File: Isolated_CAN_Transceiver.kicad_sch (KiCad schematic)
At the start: 6 parts, among them SW1 SW_DIP_x01, U4 ISO1050DUB

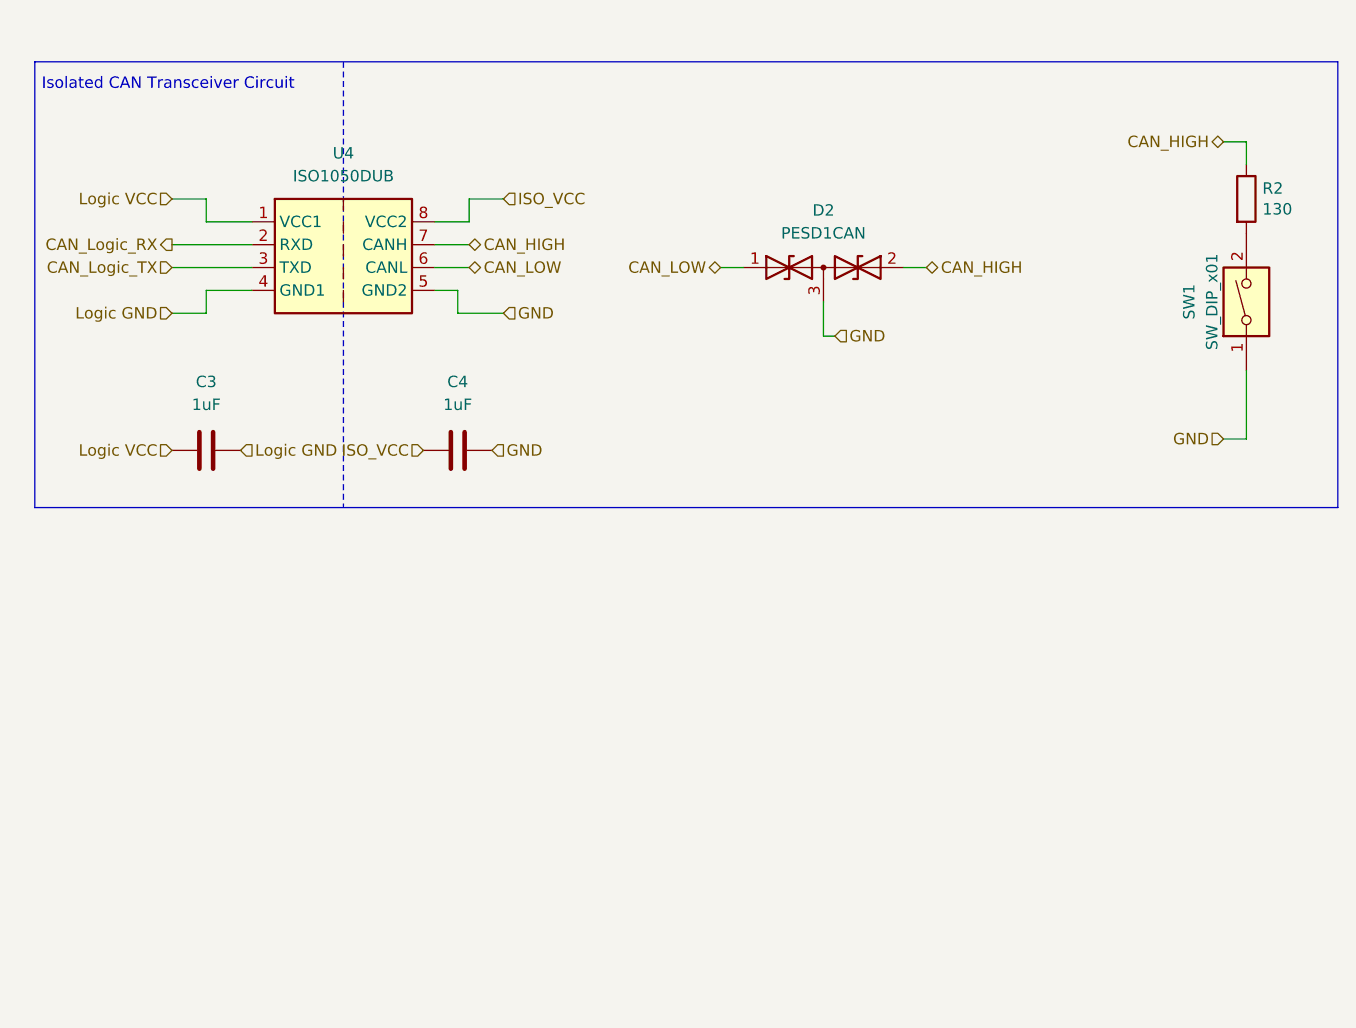
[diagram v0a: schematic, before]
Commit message: Updated Isolated CANTX
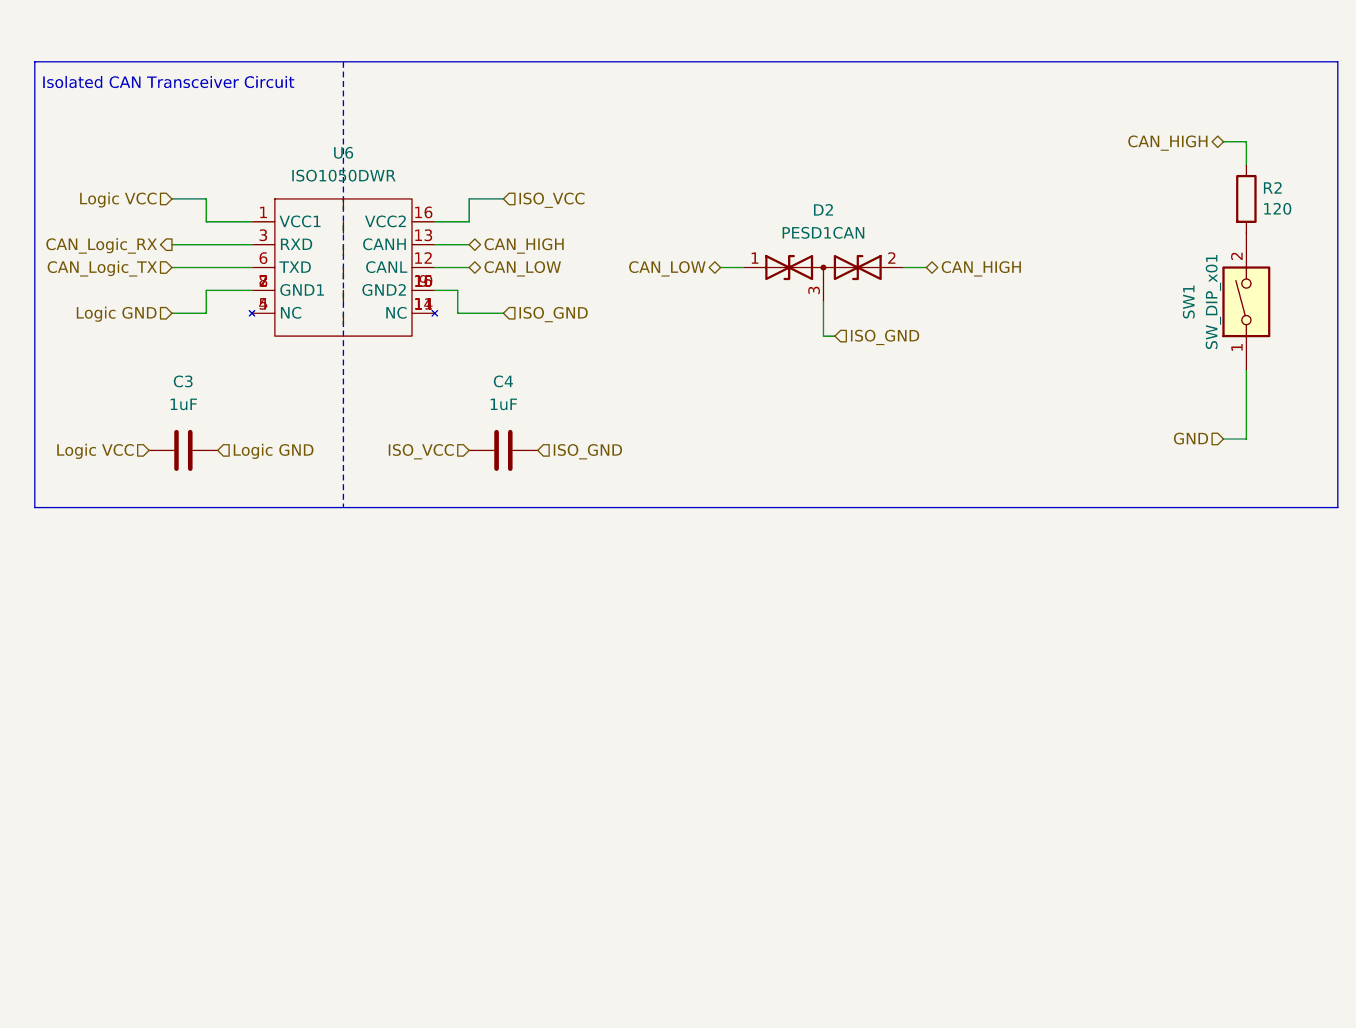
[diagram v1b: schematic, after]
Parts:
- removed U4: ISO1050DUB, Package_SO:SOP-8_6.62x9.15mm_P2.54mm, symbol Interface_CAN_LIN:ISO1050DUB
- added U6: ISO1050DWR, Package_SO:SOP-16_4.55x10.3mm_P1.27mm, symbol user:ISO1050DWR
- R2: value 130 -> 120
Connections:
- net CAN_HIGH: now also U6.13 (CANH)
- net CAN_LOW: now also U6.12 (CANL)
- net CAN_Logic_RX: now also U6.3 (RXD)
- net CAN_Logic_TX: now also U6.6 (TXD)
- net GND: no longer C4.1, D2.3 (common)
- net ISO_VCC: now also U6.16 (VCC2)
- net Logic GND: now also U6.2 (GND1), U6.7 (GND1), U6.8 (GND1)
- net Logic VCC: now also U6.1 (VCC1)
- new net: U6.11 (NC), U6.14 (NC)
- new net: U6.4 (NC), U6.5 (NC)
- new net ISO_GND: C4.1, D2.3 (common), U6.10 (GND2), U6.15 (GND2), U6.9 (GND2)
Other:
- moved on the sheet: C3, C4
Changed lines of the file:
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@@
 	(hierarchical_label "Logic VCC"
 		(shape input)
-		(at 85.09 97.79 180)
+		(at 82.55 97.79 180)
 		(effects
 			(font
@@
 		)
 	)
-	(hierarchical_label "GND"
+	(hierarchical_label "ISO_GND"
 		(shape input)
 		(at 158.75 85.09 0)
@@
 		)
 	)
-	(hierarchical_label "GND"
+	(hierarchical_label "ISO_GND"
 		(shape input)
 		(at 121.92 82.55 0)
@@
 	(hierarchical_label "ISO_VCC"
 		(shape input)
-		(at 113.03 97.79 180)
-		(effects
-			(font
-				(size 1.27 1.27)
-			)
-			(justify right)
-		)
-	)
-	(hierarchical_label "GND"
-		(shape input)
-		(at 120.65 97.79 0)
+		(at 118.11 97.79 180)
+		(effects
+			(font
+				(size 1.27 1.27)
+			)
+			(justify right)
+		)
+	)
+	(hierarchical_label "ISO_GND"
+		(shape input)
+		(at 125.73 97.79 0)
 		(effects
 			(font
@@
 	(hierarchical_label "Logic GND"
 		(shape input)
-		(at 92.71 97.79 0)
+		(at 90.17 97.79 0)
 		(effects
 			(font
@@
 	(symbol
 		(lib_id "Device:C")
-		(at 116.84 97.79 270)
+		(at 121.92 97.79 270)
 		(unit 1)
 		(exclude_from_sim no)
@@
 		(fields_autoplaced yes)
 		(property "Reference" "C4"
-			(at 116.84 90.17 90)
+			(at 121.92 90.17 90)
 			(effects
 				(font
@@
 		)
 		(property "Value" "1uF"
-			(at 116.84 92.71 90)
+			(at 121.92 92.71 90)
 			(effects
 				(font
@@
 		)
 		(property "Footprint" "Capacitor_SMD:C_0603_1608Metric"
-			(at 113.03 98.7552 0)
+			(at 118.11 98.7552 0)
 			(effects
 				(font
@@
 		)
 		(property "Datasheet" "~"
-			(at 116.84 97.79 0)
+			(at 121.92 97.79 0)
 			(effects
 				(font
@@
 		)
 		(property "Description" ""
-			(at 116.84 97.79 0)
+			(at 121.92 97.79 0)
 			(effects
 				(font
@@
 		)
 		(property "LCSC" "C15849"
-			(at 116.84 97.79 0)
+			(at 121.92 97.79 0)
 			(effects
 				(font
@@
 	)
 	(symbol
-		(lib_id "Interface_CAN_LIN:ISO1050DUB")
-		(at 104.14 74.93 0)
-		(unit 1)
-		(exclude_from_sim no)
-		(in_bom yes)
-		(on_board yes)
-		(dnp no)
-		(fields_autoplaced yes)
-		(property "Reference" "U4"
-			(at 104.14 64.77 0)
-			(effects
-				(font
-					(size 1.27 1.27)
-				)
-			)
-		)
-		(property "Value" "ISO1050DUB"
-			(at 104.14 67.31 0)
-			(effects
-				(font
-					(size 1.27 1.27)
-				)
-			)
-		)
-		(property "Footprint" "Package_SO:SOP-8_6.62x9.15mm_P2.54mm"
-			(at 104.14 83.82 0)
-			(effects
-				(font
-					(size 1.27 1.27)
-					(italic yes)
-				)
-				(hide yes)
-			)
-		)
-		(property "Datasheet" "http://www.ti.com/lit/ds/symlink/iso1050.pdf"
-			(at 104.14 76.2 0)
-			(effects
-				(font
-					(size 1.27 1.27)
-				)
-				(hide yes)
-			)
-		)
-		(property "Description" "Isolated CAN Transceiver, SOP-8"
-			(at 104.14 74.93 0)
-			(effects
-				(font
-					(size 1.27 1.27)
-				)
-				(hide yes)
-			)
-		)
-		(pin "3"
-		)
-		(pin "1"
-		)
-		(pin "2"
-		)
-		(pin "4"
-		)
-		(pin "7"
-		)
-		(pin "8"
-		)
-		(pin "6"
-		)
-		(pin "5"
-		)
-		(instances
-			(project "BMS"
-				(path "/d7e219ab-f530-45f5-8a23-0e6b6d2e3e0f/aff9ba91-cad3-4d4c-9149-201fa529c26c"
-					(reference "U4")
-					(unit 1)
-				)
-			)
-		)
-	)
-	(symbol
 		(lib_id "Device:C")
-		(at 88.9 97.79 270)
+		(at 86.36 97.79 270)
 		(unit 1)
 		(exclude_from_sim no)
@@
 		(fields_autoplaced yes)
 		(property "Reference" "C3"
-			(at 88.9 90.17 90)
+			(at 86.36 90.17 90)
 			(effects
 				(font
@@
 		)
 		(property "Value" "1uF"
-			(at 88.9 92.71 90)
+			(at 86.36 92.71 90)
 			(effects
 				(font
@@
 		)
 		(property "Footprint" "Capacitor_SMD:C_0603_1608Metric"
-			(at 85.09 98.7552 0)
+			(at 82.55 98.7552 0)
 			(effects
 				(font
@@
 		)
 		(property "Datasheet" "~"
-			(at 88.9 97.79 0)
+			(at 86.36 97.79 0)
 			(effects
 				(font
@@
 		)
 		(property "Description" ""
-			(at 88.9 97.79 0)
+			(at 86.36 97.79 0)
 			(effects
 				(font
@@
 		)
 		(property "LCSC" "C15849"
-			(at 88.9 97.79 0)
+			(at 86.36 97.79 0)
 			(effects
 				(font
@@
 			)
 		)
-		(property "Value" "130"
+		(property "Value" "120"
 			(at 206.248 70.993 0)
 			(effects
@@
 					(unit 1)
 				)
+			)
+		)
+	)
+	(symbol
+		(lib_id "user:ISO1050DWR")
+		(at 104.14 74.93 0)
+		(unit 1)
+		(exclude_from_sim no)
+		(in_bom yes)
+		(on_board yes)
+		(dnp no)
+		(fields_autoplaced yes)
+		(property "Reference" "U6"
+			(at 104.14 64.77 0)
+			(effects
+				(font
+					(size 1.27 1.27)
+				)
+			)
+		)
+		(property "Value" "ISO1050DWR"
+			(at 104.14 67.31 0)
+			(effects
+				(font
+					(size 1.27 1.27)
+				)
+			)
+		)
+		(property "Footprint" "Package_SO:SOP-16_4.55x10.3mm_P1.27mm"
+			(at 104.14 87.122 0)
+			(effects
+				(font
+					(size 1.27 1.27)
+					(italic yes)
+				)
+				(hide yes)
+			)
+		)
+		(property "Datasheet" "https://www.ti.com/lit/ds/symlink/iso1050.pdf"
+			(at 102.87 64.262 0)
+			(effects
+				(font
+					(size 1.27 1.27)
+				)
+				(hide yes)
+			)
+		)
+		(property "Description" "Isolated CAN Transceiver, SOP-16"
+			(at 102.616 66.294 0)
+			(effects
+				(font
+					(size 1.27 1.27)
+				)
+				(hide yes)
+			)
+		)
+		(property "LCSC" "C93718"
+			(at 104.14 74.93 0)
+			(effects
+				(font
+					(size 1.27 1.27)
+				)
+				(hide yes)
+			)
+		)
+		(pin "14"
+		)
+		(pin "15"
+		)
+		(pin "9"
+		)
+		(pin "11"
+		)
+		(pin "10"
+		)
+		(pin "6"
+		)
+		(pin "5"
+		)
+		(pin "12"
+		)
+		(pin "1"
+		)
+		(pin "3"
+		)
+		(pin "2"
+		)
+		(pin "4"
+		)
+		(pin "7"
+		)
+		(pin "8"
+		)
+		(pin "16"
+		)
+		(pin "13"
+		)
+		(instances
+			(project "BMS"
+				(path "/d7e219ab-f530-45f5-8a23-0e6b6d2e3e0f/aff9ba91-cad3-4d4c-9149-201fa529c26c"
+					(reference "U6")
+					(unit 1)
+				)

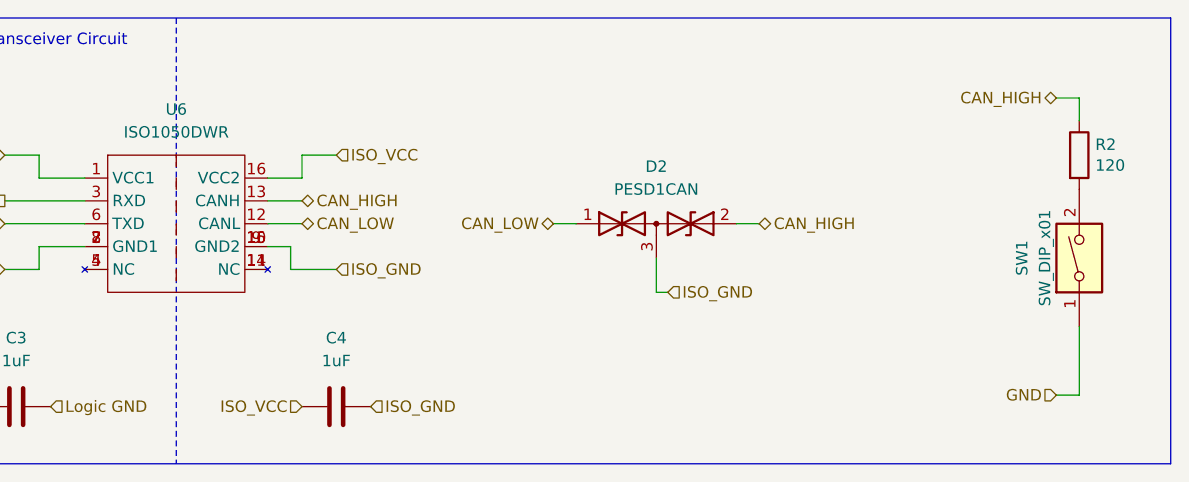
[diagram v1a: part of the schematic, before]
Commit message: Connectors, high side circuits added, layout progressed
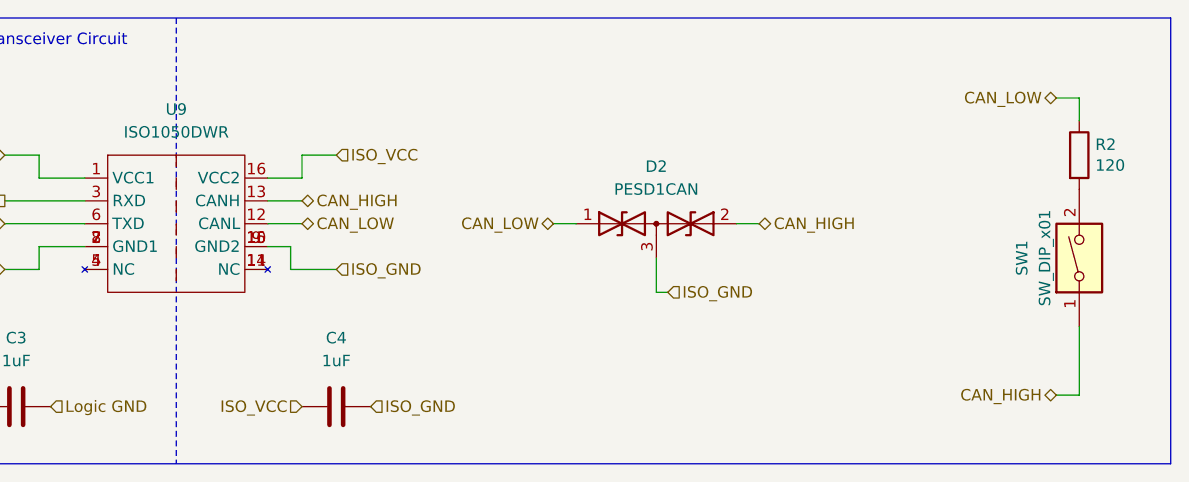
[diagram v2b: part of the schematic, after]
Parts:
- renumbered U6 to U9
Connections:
- net GND is gone; now on net CAN_HIGH: SW1.1
- net CAN_HIGH: no longer R2.1
- net CAN_LOW: now also R2.1
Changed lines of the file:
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@@
-		)
-	)
-	(hierarchical_label "GND"
-		(shape input)
-		(at 201.93 96.52 180)
-		(effects
-			(font
-				(size 1.27 1.27)
-			)
-			(justify right)
 		)
 	)
@@
 	(hierarchical_label "CAN_HIGH"
 		(shape bidirectional)
+		(at 201.93 96.52 180)
+		(effects
+			(font
+				(size 1.27 1.27)
+			)
+			(justify right)
+		)
+	)
+	(hierarchical_label "Logic VCC"
+		(shape input)
+		(at 85.09 69.85 180)
+		(effects
+			(font
+				(size 1.27 1.27)
+			)
+			(justify right)
+		)
+	)
+	(hierarchical_label "CAN_LOW"
+		(shape bidirectional)
 		(at 201.93 63.5 180)
-		(effects
-			(font
-				(size 1.27 1.27)
-			)
-			(justify right)
-		)
-	)
-	(hierarchical_label "Logic VCC"
-		(shape input)
-		(at 85.09 69.85 180)
 		(effects
 			(font
@@
 		(dnp no)
 		(fields_autoplaced yes)
-		(property "Reference" "U6"
+		(property "Reference" "U9"
 			(at 104.14 64.77 0)
 			(effects
@@
 			(project "BMS"
 				(path "/d7e219ab-f530-45f5-8a23-0e6b6d2e3e0f/aff9ba91-cad3-4d4c-9149-201fa529c26c"
-					(reference "U6")
+					(reference "U9")
 					(unit 1)
 				)

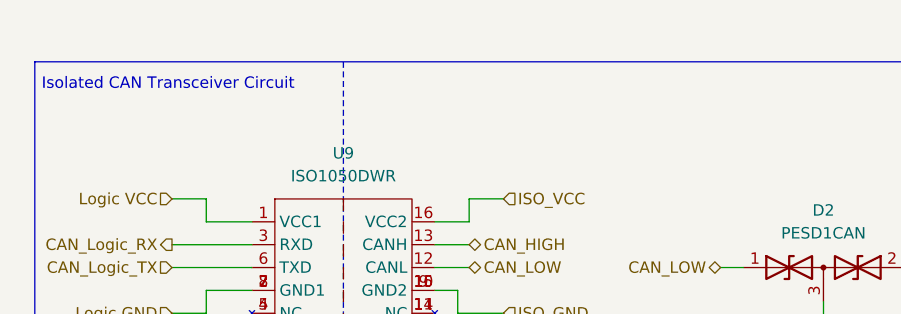
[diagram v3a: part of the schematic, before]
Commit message: Finalised RS485 Circuit, Layout improvemnts, mounting holes, silkscreen...
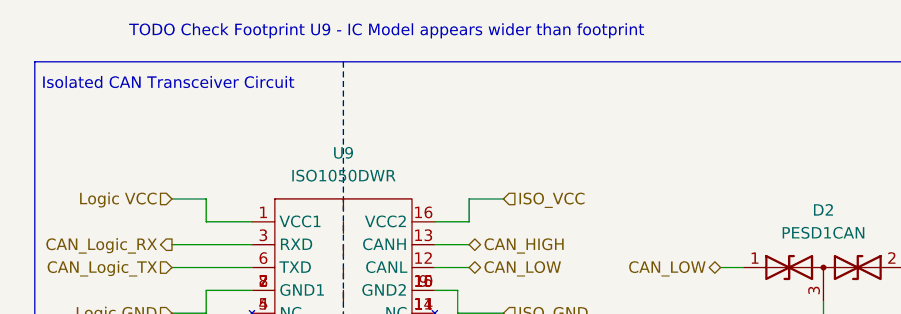
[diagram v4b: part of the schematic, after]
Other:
- note added: "TODO Check Footprint U9 - IC Model appears wider than footprint"
- company: (none) -> eChook
- title: (none) -> BMS Comms Master Board
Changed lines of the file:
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@@
 	(generator_version "9.0")
 	(paper "A4")
+	(title_block
+		(title "BMS Comms Master Board")
+		(date "2025-05-21")
+		(rev "0.1")
+		(company "eChook")
+	)
+	(text "TODO Check Footprint U9 - IC Model appears wider than footprint"
+		(exclude_from_sim no)
+		(at 108.966 51.308 0)
+		(effects
+			(font
+				(size 1.27 1.27)
+			)
+		)
+	)
 	(text "Isolated CAN Transceiver Circuit"
 		(exclude_from_sim no)

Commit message: ISOCAN footprint update, zone optimisations
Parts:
- U9: footprint Package_SO:SOP-16_4.55x10.3mm_P1.27mm -> Package_SO:SOIC-16W_7.5x10.3mm_P1.27mm
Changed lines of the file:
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@@
 			)
 		)
-		(property "Footprint" "Package_SO:SOP-16_4.55x10.3mm_P1.27mm"
+		(property "Footprint" "Package_SO:SOIC-16W_7.5x10.3mm_P1.27mm"
 			(at 104.14 87.122 0)
 			(effects

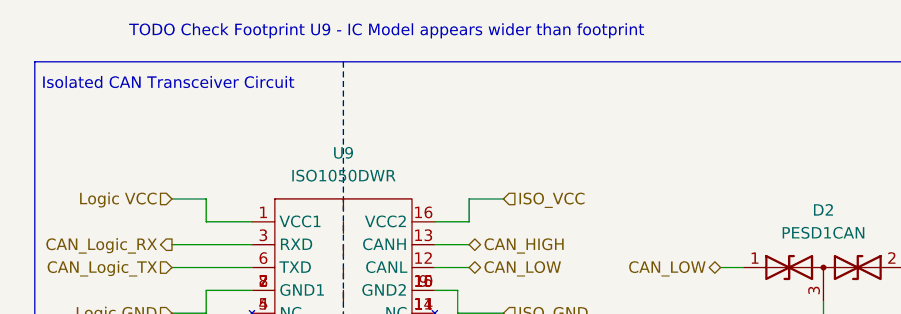
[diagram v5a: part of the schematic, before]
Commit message: Schematic Net Colours
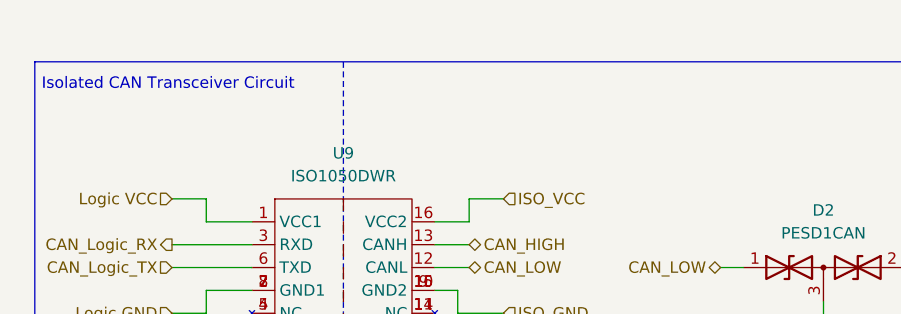
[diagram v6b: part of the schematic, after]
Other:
- note removed: "TODO Check Footprint U9 - IC Model appears wider than footprint"
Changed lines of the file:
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@@
 		(company "eChook")
-	)
-	(text "TODO Check Footprint U9 - IC Model appears wider than footprint"
-		(exclude_from_sim no)
-		(at 108.966 51.308 0)
-		(effects
-			(font
-				(size 1.27 1.27)
-			)
-		)
 	)
 	(text "Isolated CAN Transceiver Circuit"

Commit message: Implemented schematic review suggestions (Notes.txt)
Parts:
- R2: footprint Resistor_SMD:R_0603_1608Metric -> Resistor_SMD:R_0805_2012Metric; LCSC (none) -> C543533
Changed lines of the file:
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@@
 			)
 		)
-		(property "Datasheet" "~"
+		(property "Datasheet" "https://lcsc.com/datasheet/lcsc_datasheet_2411201840_DEALON-SP-01P_C5160893.pdf"
 			(at 204.47 81.28 0)
 			(effects
@@
 			)
 		)
-		(property "Footprint" "Resistor_SMD:R_0603_1608Metric"
+		(property "Footprint" "Resistor_SMD:R_0805_2012Metric"
 			(at 202.692 69.85 90)
 			(effects
@@
 			)
 		)
-		(property "Description" ""
+		(property "Description" "CAN Termination Resistor 1/2W"
 			(at 204.47 69.85 0)
 			(effects
@@
 			)
 		)
-		(property "LCSC" ""
+		(property "LCSC" "C543533"
 			(at 204.47 69.85 0)
 			(effects

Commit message: Pinout Review Complete, Altenative option for ISO CAN IC added
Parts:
- added U21: ISO1050DUB, Package_SO:SOP-8_6.62x9.15mm_P2.54mm, symbol Interface_CAN_LIN:ISO1050DUB
- U9: now not fitted; now left out of the parts list
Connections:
- net CAN_HIGH: now also U9.14 (NC), U21.7 (CANH)
- net CAN_LOW: now also U21.6 (CANL)
- net CAN_Logic_RX: now also U21.2 (RXD)
- net CAN_Logic_TX: now also U9.5 (NC), U21.3 (TXD)
- net ISO_GND: now also U21.5 (GND2)
- net ISO_VCC: now also U21.8 (VCC2)
- net Logic GND: now also U21.4 (GND1)
- net Logic VCC: now also U21.1 (VCC1)
- net at U9.11 (NC): no longer U9.14 (NC)
- net at U9.4 (NC): no longer U9.5 (NC)
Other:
- note added: "Alternative CAN Driver -DWB"
